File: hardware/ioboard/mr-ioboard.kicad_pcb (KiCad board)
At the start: 0 parts

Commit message: Initial IO board layout
Signed-off-by: gatecat <gatecat@ds0.me>
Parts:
- added AE1: Antenna_Chip, RF_Antenna:Johanson_2450AT43F0100, F.Cu at (105.0, 57.0)
- added C1: 10µ, Capacitor_SMD:C_0805_2012Metric, F.Cu at (120.5, 84.0)
- added C10: 10µ, Capacitor_SMD:C_0805_2012Metric, F.Cu at (111.0, 88.5)
- added C11: 100p, Capacitor_SMD:C_0402_1005Metric, F.Cu at (123.5, 103.0)
- added C12: 1µ, Capacitor_SMD:C_0603_1608Metric, F.Cu at (108.0, 116.5)
- added C13: 10µ, Capacitor_SMD:C_0805_2012Metric, F.Cu at (123.0, 93.0)
- added C14: 10µ, Capacitor_SMD:C_0805_2012Metric, F.Cu at (114.3, 100.5)
- added C15: 10µ, Capacitor_SMD:C_0805_2012Metric, F.Cu at (123.0, 84.0)
- added C16: 10µ, Capacitor_SMD:C_0805_2012Metric, F.Cu at (116.8, 100.5)
- added C17: 10µ, Capacitor_SMD:C_0805_2012Metric, F.Cu at (111.8, 100.5)
- added C18: 470n, Capacitor_SMD:C_0402_1005Metric, F.Cu at (138.5, 69.0)
- added C19: 470n, Capacitor_SMD:C_0402_1005Metric, F.Cu at (136.5, 76.5)
- added C2: 10µ/25V, Capacitor_SMD:C_0805_2012Metric, F.Cu at (125.5, 108.0)
- added C20: 470n, Capacitor_SMD:C_0402_1005Metric, F.Cu at (142.5, 86.5)
- added C21: 10n, Capacitor_SMD:C_0402_1005Metric, F.Cu at (159.5, 89.0)
- added C22: 10µ, Capacitor_SMD:C_0805_2012Metric, F.Cu at (155.5, 92.0)
- added C23: 200p, Capacitor_SMD:C_0402_1005Metric, F.Cu at (135.5, 115.5)
- added C24: 200p, Capacitor_SMD:C_0402_1005Metric, F.Cu at (135.5, 114.0)
- added C25: 10µ, Capacitor_SMD:C_0805_2012Metric, F.Cu at (113.5, 80.0)
- added C26: 10µ, Capacitor_SMD:C_0805_2012Metric, F.Cu at (111.0, 80.0)
- added C27: 10p, Capacitor_SMD:C_0402_1005Metric, F.Cu at (111.0, 64.5)
- added C28: 1p, Capacitor_SMD:C_0402_1005Metric, F.Cu at (109.0, 65.0)
- added C29: 1.2p, Capacitor_SMD:C_0402_1005Metric, F.Cu at (106.0, 65.0)
- added C3: 10µ, Capacitor_SMD:C_0805_2012Metric, F.Cu at (120.5, 93.0)
- added C30: 10µ, Capacitor_SMD:C_0805_2012Metric, F.Cu at (150.5, 99.5)
- added C31: 10µ, Capacitor_SMD:C_0805_2012Metric, F.Cu at (149.0, 96.0)
- added C32: 10µ, Capacitor_SMD:C_0805_2012Metric, F.Cu at (150.6, 93.0)
- added C33: 470n, Capacitor_SMD:C_0402_1005Metric, F.Cu at (132.5, 103.5)
- added C34: 470n, Capacitor_SMD:C_0402_1005Metric, F.Cu at (128.5, 94.5)
- added C35: 470n, Capacitor_SMD:C_0402_1005Metric, F.Cu at (145.5, 87.0)
- added C36: 470n, Capacitor_SMD:C_0402_1005Metric, F.Cu at (128.5, 91.5)
- added C37: 470n, Capacitor_SMD:C_0402_1005Metric, F.Cu at (146.0, 96.0)
- added C38: 470n, Capacitor_SMD:C_0402_1005Metric, F.Cu at (134.5, 86.5)
- added C39: 470n, Capacitor_SMD:C_0402_1005Metric, F.Cu at (146.5, 92.0)
- added C4: 10µ/25V, Capacitor_SMD:C_0805_2012Metric, F.Cu at (124.5, 112.0)
- added C40: 470n, Capacitor_SMD:C_0402_1005Metric, F.Cu at (145.0, 100.5)
- added C41: 470n, Capacitor_SMD:C_0402_1005Metric, F.Cu at (148.0, 99.5)
- added C42: 470n, Capacitor_SMD:C_0402_1005Metric, F.Cu at (132.5, 102.5)
- added C43: 470n, Capacitor_SMD:C_0402_1005Metric, F.Cu at (128.5, 92.5)
- added C44: 10µ, Capacitor_SMD:C_0805_2012Metric, F.Cu at (151.5, 96.0)
- added C45: 470n, Capacitor_SMD:C_0402_1005Metric, F.Cu at (128.5, 95.5)
- added C46: 10µ, Capacitor_SMD:C_0805_2012Metric, F.Cu at (133.5, 80.5)
- added C47: 10µ, Capacitor_SMD:C_0805_2012Metric, F.Cu at (129.0, 84.0)
- added C48: 1µ, Capacitor_SMD:C_0603_1608Metric, F.Cu at (128.5, 97.0)
- added C49: 1u, Capacitor_SMD:C_0603_1608Metric, F.Cu at (149.5, 89.0)
- added C5: 22µ, Capacitor_Tantalum_SMD:CP_EIA-3528-12_Kemet-T, F.Cu at (108.0, 123.0)
- added C50: 1u, Capacitor_SMD:C_0603_1608Metric, F.Cu at (149.5, 85.0)
- added C51: 10µ, Capacitor_SMD:C_0805_2012Metric, F.Cu at (150.6, 103.0)
- added C6: 470n, Capacitor_SMD:C_0402_1005Metric, F.Cu at (138.5, 64.0)
- added C7: 470n, Capacitor_SMD:C_0402_1005Metric, F.Cu at (138.0, 76.5)
- added C8: 10µ, Capacitor_SMD:C_0805_2012Metric, F.Cu at (113.5, 88.5)
- added C9: 100n/25V, Capacitor_SMD:C_0402_1005Metric, F.Cu at (120.0, 112.5)
- added D1: LED_Small, LED_SMD:LED_0805_2012Metric, F.Cu at (138.0, 53.0)
- added D2: LED_Small, LED_SMD:LED_0805_2012Metric, F.Cu at (141.0, 53.0)
- added D3: LED_Small, LED_SMD:LED_0805_2012Metric, F.Cu at (144.0, 53.0)
- added D4: LED_Small, LED_SMD:LED_0805_2012Metric, F.Cu at (153.0, 53.0)
- added FB1: FerriteBead_Small, Inductor_SMD:L_0603_1608Metric, F.Cu at (154.7, 99.5)
- added J1: Conn_01x40_Shielded, meowality:TE_FPC_40pin_p0.5mm_4-1734839-0, F.Cu at (160.0, 70.0)
- added J2: USB_C_Receptacle_USB2.0, Connector_USB:USB_C_Receptacle_GCT_USB4085, F.Cu at (115.0, 124.0)
- added J3: Conn_01x06, Connector_PinHeader_2.54mm:PinHeader_1x06_P2.54mm_Vertical, F.Cu at (103.0, 81.5)
- added J4: Micro_SD_Card_Det, Connector_Card:microSD_HC_Hirose_DM3BT-DSF-PEJS, F.Cu at (155.0, 120.0)
- added J5: Conn_01x04, Connector_PinHeader_2.54mm:PinHeader_1x04_P2.54mm_Vertical, F.Cu at (103.0, 100.0)
- added JP1: CS, Jumper:SolderJumper-3_P1.3mm_Bridged12_Pad1.0x1.5mm, F.Cu at (107.2, 72.0)
- added L1: XFL4015-471MEB, Inductor_SMD:L_Coilcraft_XxL4020, F.Cu at (112.0, 93.0)
- added L2: 2.2u, Inductor_SMD:L_Bourns_SRP7028A_7.3x6.6mm, F.Cu at (115.0, 108.0)
- added L3: XFL4015-471MEB, Inductor_SMD:L_Coilcraft_XxL4020, F.Cu at (112.0, 84.2)
- added L4: 2.7n, Inductor_SMD:L_0402_1005Metric, F.Cu at (107.5, 64.5)
- added MOD1: RTL8189ES_MOD, meowality:RTL8189ES_MOD, F.Cu at (129.5, 73.2)
- added Q1: 2N7002, Package_TO_SOT_SMD:SOT-23, F.Cu at (150.0, 60.0)
- added R1: 10k, Resistor_SMD:R_0402_1005Metric, F.Cu at (117.0, 96.0)
- added R10: 0, Resistor_SMD:R_0402_1005Metric, F.Cu at (119.5, 103.0)
- added R11: 45.3k, Resistor_SMD:R_0402_1005Metric, F.Cu at (120.5, 103.0)
- added R12: 10k, Resistor_SMD:R_0402_1005Metric, F.Cu at (125.5, 103.5)
- added R13: 10k, Resistor_SMD:R_0402_1005Metric, F.Cu at (154.0, 75.5)
- added R14: 10k, Resistor_SMD:R_0402_1005Metric, F.Cu at (135.0, 73.0)
- added R15: 10k, Resistor_SMD:R_0402_1005Metric, F.Cu at (117.0, 86.5)
- added R16: 2.2k, Resistor_SMD:R_0402_1005Metric, F.Cu at (136.0, 122.5)
- added R17: 2.2k, Resistor_SMD:R_0402_1005Metric, F.Cu at (136.0, 123.5)
- added R18: 2.2k, Resistor_SMD:R_0402_1005Metric, F.Cu at (136.0, 124.5)
- added R19: 8.45k, Resistor_SMD:R_0402_1005Metric, F.Cu at (117.0, 79.0)
- added R2: NC, Resistor_SMD:R_0402_1005Metric, F.Cu at (125.5, 105.0)
- added R20: 10k, Resistor_SMD:R_0402_1005Metric, F.Cu at (117.0, 80.5)
- added R21: 10k, Resistor_SMD:R_0402_1005Metric, F.Cu at (146.0, 59.0)
- added R22: 2.2k, Resistor_SMD:R_0402_1005Metric, F.Cu at (154.0, 57.5)
- added R23: 75, Resistor_SMD:R_0402_1005Metric, F.Cu at (146.5, 94.0)
- added R24: 75, Resistor_SMD:R_0402_1005Metric, F.Cu at (146.5, 93.0)
- added R25: 2.2k, Resistor_SMD:R_0402_1005Metric, F.Cu at (128.0, 87.0)
- added R26: 2.2k, Resistor_SMD:R_0402_1005Metric, F.Cu at (129.0, 87.0)
- added R27: 200k, Resistor_SMD:R_0402_1005Metric, F.Cu at (149.5, 87.5)
- added R28: 200k, Resistor_SMD:R_0402_1005Metric, F.Cu at (149.5, 86.5)
- added R3: 2.2k, Resistor_SMD:R_0402_1005Metric, F.Cu at (138.0, 58.5)
- added R4: 2.2k, Resistor_SMD:R_0402_1005Metric, F.Cu at (141.0, 58.5)
- added R5: 15k, Resistor_SMD:R_0402_1005Metric, F.Cu at (117.0, 89.0)
- added R6: 10k, Resistor_SMD:R_0402_1005Metric, F.Cu at (117.0, 90.5)
- added R7: 2.2k, Resistor_SMD:R_0402_1005Metric, F.Cu at (144.0, 58.5)
- added R8: 0, Resistor_SMD:R_0402_1005Metric, F.Cu at (120.0, 113.5)
- added R9: 20k, Resistor_SMD:R_0402_1005Metric, F.Cu at (122.5, 103.0)
- added RN1: 47k, Resistor_SMD:R_Array_Convex_4x0402, F.Cu at (161.5, 103.5)
- added RN2: 47k, Resistor_SMD:R_Array_Convex_4x0402, F.Cu at (161.5, 108.5)
- added RN3: 47k, Resistor_SMD:R_Array_Convex_4x0402, F.Cu at (135.0, 70.2)
- added RN4: 47k, Resistor_SMD:R_Array_Convex_4x0402, F.Cu at (135.0, 63.8)
- added SW1: SW_Push, Button_Switch_SMD:SW_SPST_B3U-1000P, F.Cu at (103.0, 115.0)
- added TP1: EN, TestPoint:TestPoint_Pad_D2.0mm, F.Cu at (129.0, 105.5)
- added TP2: TestPoint, TestPoint:TestPoint_Pad_D2.0mm, F.Cu at (129.5, 126.0)
- added U1: TPS62822, meowality:TI_VSON-HR_1.5x2mm_p0.5mm, F.Cu at (117.0, 93.0)
- added U10: F1C200S, meowality:QFN-88_EP_10x10_Pitch0.4mm, F.Cu at (138.2, 94.2)
- added U2: TPS56637, meowality:VQFN10-HR, F.Cu at (122.0, 108.0)
- added U3: TPD2E2U06, Package_TO_SOT_SMD:SOT-553, F.Cu at (116.0, 119.5)
- added U4: DS90C363, Package_SO:TSSOP-48_8x12.5mm_P0.5mm, F.Cu at (146.0, 71.0)
- added U5: TPD2E2U06, Package_TO_SOT_SMD:SOT-553, F.Cu at (120.0, 119.5)
- added U6: LD3985M28R_SOT23, Package_TO_SOT_SMD:SOT-23-5, F.Cu at (159.5, 92.0)
- added U7: TPS62822, meowality:TI_VSON-HR_1.5x2mm_p0.5mm, F.Cu at (117.0, 84.0)
- added U8: FUSB302BMPX, Package_DFN_QFN:WQFN-14-1EP_2.5x2.5mm_P0.5mm_EP1.45x1.45mm, F.Cu at (133.0, 119.0)
- added U9: TPD2E2U06, Package_TO_SOT_SMD:SOT-553, F.Cu at (126.5, 119.5)
- added Y1: 24MHz, Oscillator:Oscillator_SMD_EuroQuartz_XO32-4Pin_3.2x2.5mm, F.Cu at (137.0, 103.5)
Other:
- board outline added: 65 x 80 mm
- copper layers 0 -> 2

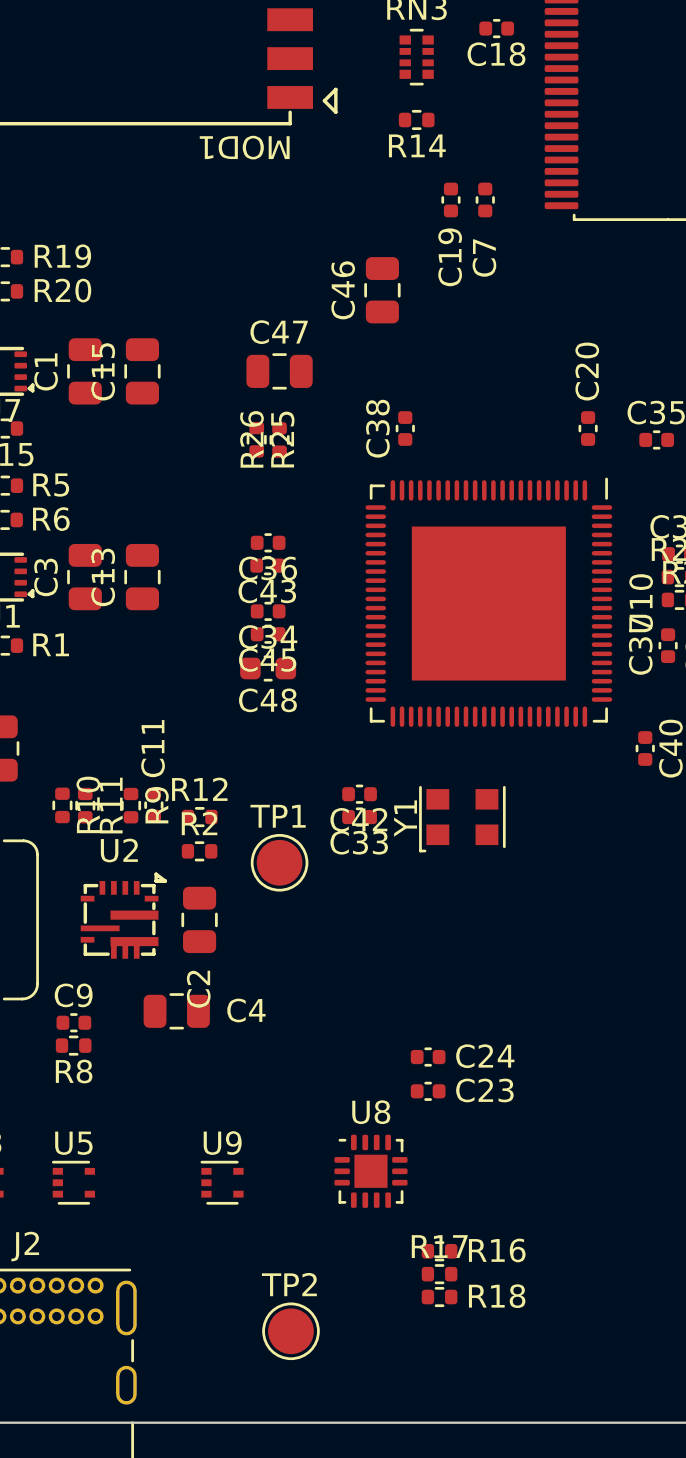
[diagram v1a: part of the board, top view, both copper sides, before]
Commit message: Add a few missing parts to IO board
Signed-off-by: gatecat <gatecat@ds0.me>
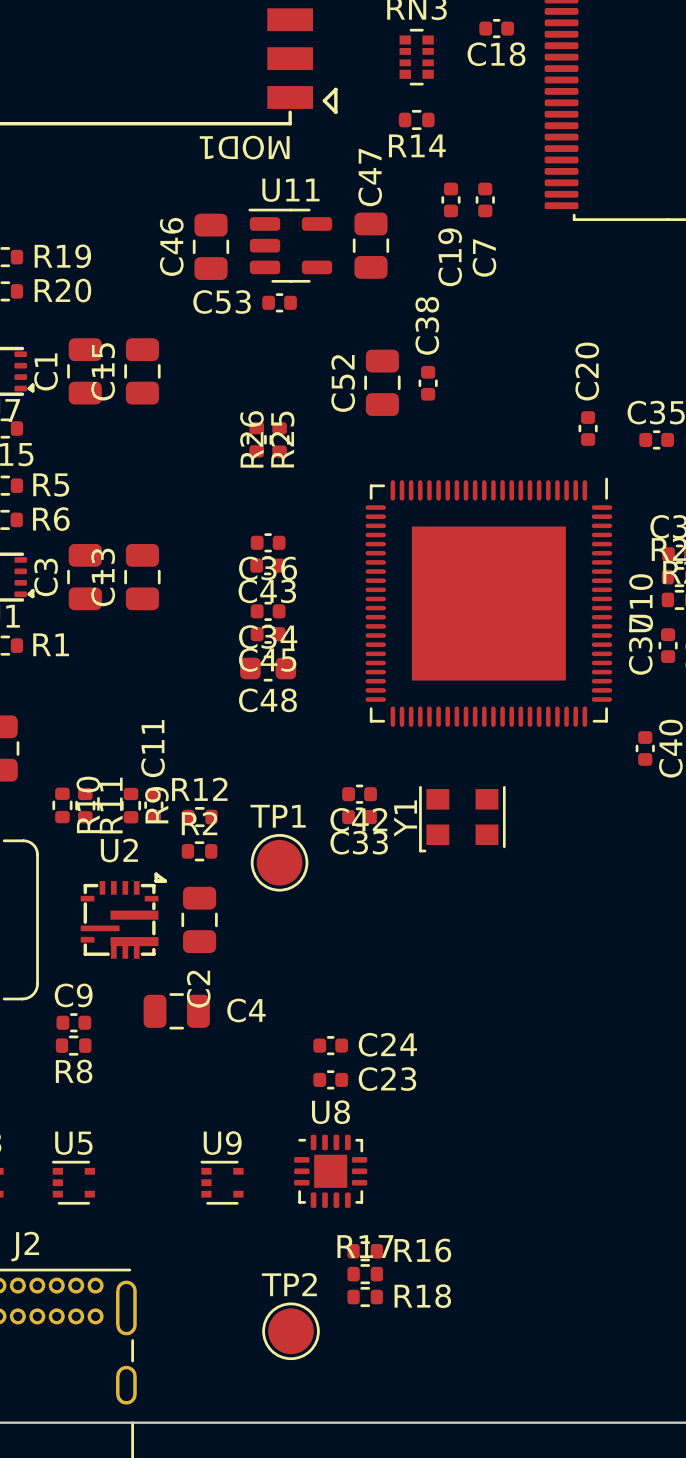
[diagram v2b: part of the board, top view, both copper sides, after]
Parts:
- added C52: 10µ, Capacitor_SMD:C_0805_2012Metric, F.Cu at (133.5, 84.5)
- added C53: 10n, Capacitor_SMD:C_0402_1005Metric, F.Cu at (129.0, 81.0)
- added U11: LD3985M25R_SOT23, Package_TO_SOT_SMD:SOT-23-5, F.Cu at (129.5, 78.5)
- moved C46 7.74 mm to (126.0, 78.5)
- moved C47 6.80 mm to (133.0, 78.5), turned to -90 degrees
- moved C23 4.29 mm to (131.2, 115.0)
- moved C24 4.29 mm to (131.2, 113.5)
- moved R16 3.25 mm to (132.7, 122.5)
- moved R17 3.25 mm to (132.7, 123.5)
- moved R18 3.25 mm to (132.7, 124.5)
- moved C38 2.22 mm to (135.5, 84.5)
- moved U8 1.76 mm to (131.2, 119.0)

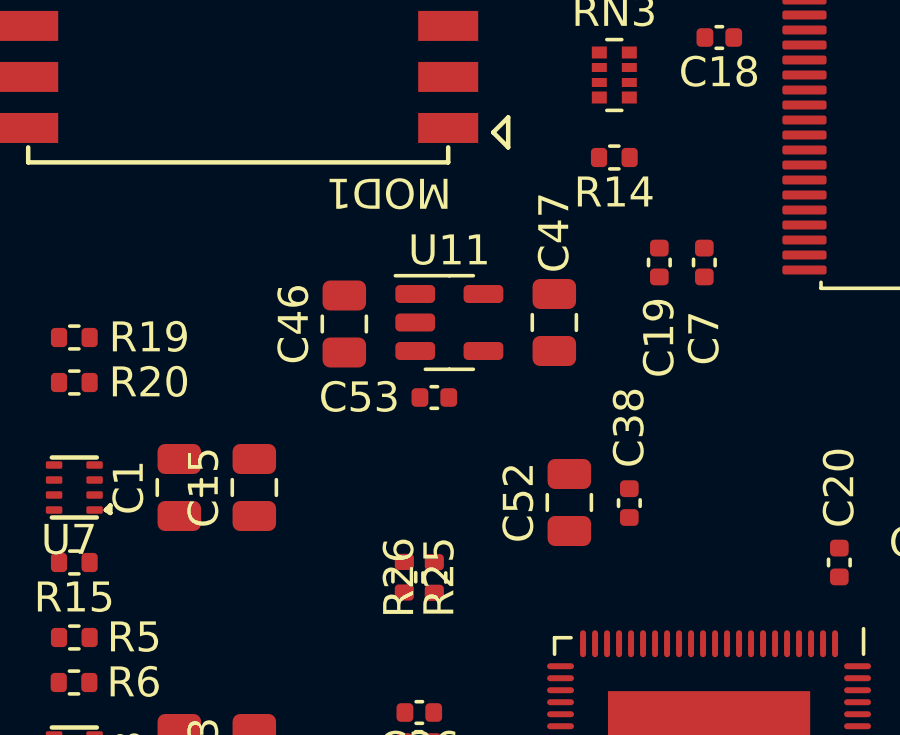
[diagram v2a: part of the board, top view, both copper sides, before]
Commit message: Fix IO board 2.5V supply
Signed-off-by: gatecat <gatecat@ds0.me>
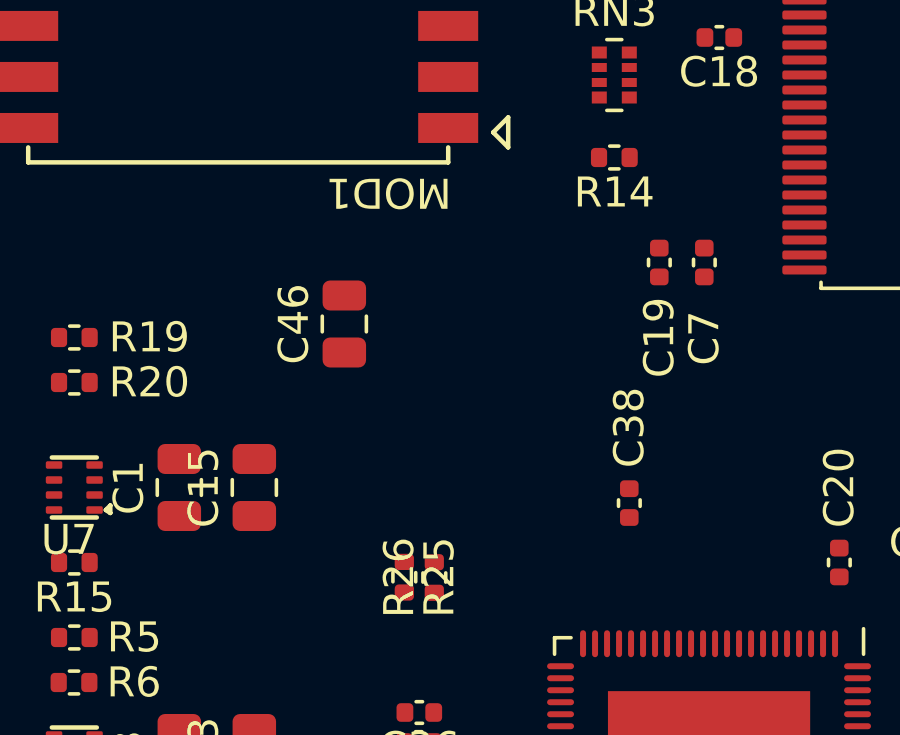
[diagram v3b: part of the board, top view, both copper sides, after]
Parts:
- removed C47, C52: 10µ, Capacitor_SMD:C_0805_2012Metric
- removed C53: 10n, Capacitor_SMD:C_0402_1005Metric
- removed U11: LD3985M25R_SOT23, Package_TO_SOT_SMD:SOT-23-5
- R5: value 15k -> 31.6k
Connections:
- C10 pad 1: +1V5 -> +2V5
- C8 pad 1: +1V5 -> +2V5
- L1 pad 2: +1V5 -> +2V5
- R5 pad 1: +1V5 -> +2V5

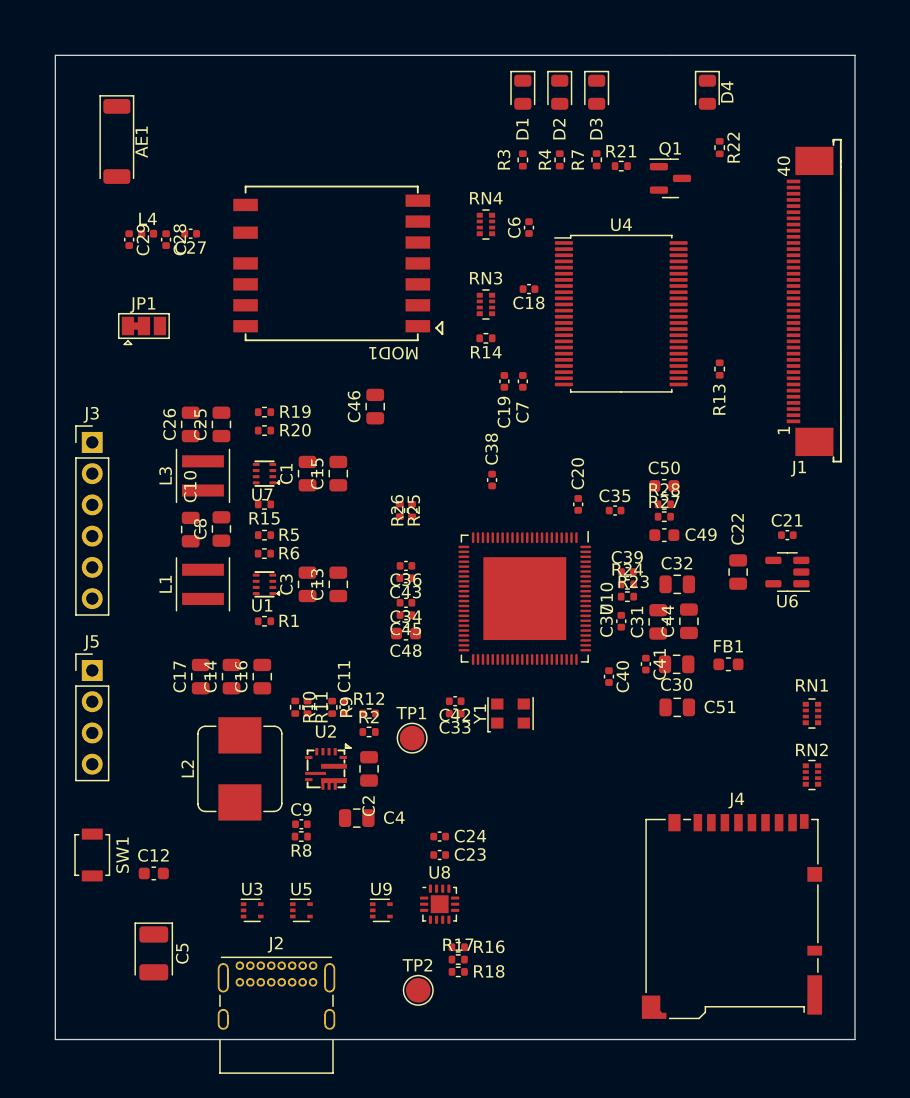
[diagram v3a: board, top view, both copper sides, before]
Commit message: Add VLED buck regulator to IO board
Signed-off-by: gatecat <gatecat@ds0.me>
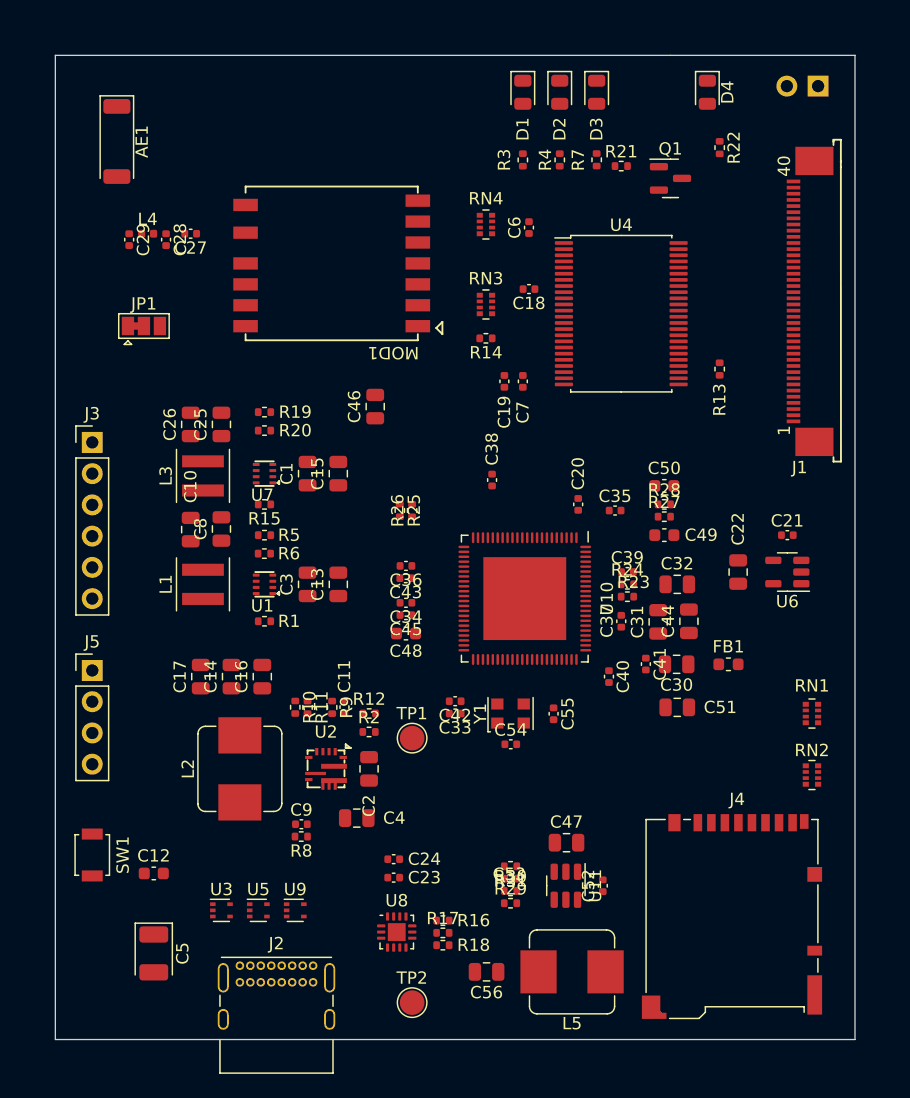
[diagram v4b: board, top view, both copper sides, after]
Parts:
- added C47: 10µ/25V, Capacitor_SMD:C_0805_2012Metric, F.Cu at (141.6, 114.0)
- added C52: 100n, Capacitor_SMD:C_0402_1005Metric, F.Cu at (144.5, 117.5)
- added C53: 100p, Capacitor_SMD:C_0402_1005Metric, F.Cu at (137.0, 116.9)
- added C54: 12p, Capacitor_SMD:C_0402_1005Metric, F.Cu at (137.0, 106.0)
- added C55: 12p, Capacitor_SMD:C_0402_1005Metric, F.Cu at (140.5, 103.5)
- added C56: 10µ, Capacitor_SMD:C_0805_2012Metric, F.Cu at (135.1, 124.5)
- added J6: Conn_01x02, Connector_PinHeader_2.54mm:PinHeader_1x02_P2.54mm_Vertical, B.Cu at (162.0, 52.5)
- added L5: 15u, Inductor_SMD:L_Bourns_SRP7028A_7.3x6.6mm, F.Cu at (142.0, 124.5)
- added R29: 49.9, Resistor_SMD:R_0402_1005Metric, F.Cu at (137.0, 118.9)
- added R30: 100k, Resistor_SMD:R_0402_1005Metric, F.Cu at (137.0, 117.9)
- added R31: 13.3k, Resistor_SMD:R_0402_1005Metric, F.Cu at (137.0, 115.9)
- added U11: TPS54202DDC, Package_TO_SOT_SMD:SOT-23-6, F.Cu at (141.5, 117.5)
- moved U9 7.00 mm to (119.5, 119.5)
- moved C23 4.17 mm to (127.5, 116.8)
- moved C24 4.17 mm to (127.5, 115.3)
- moved U8 4.16 mm to (127.8, 121.3)
- moved U5 3.50 mm to (116.5, 119.5)
- moved R16 2.50 mm to (131.5, 120.3)
- moved R17 2.50 mm to (131.5, 121.3)
- moved R18 2.50 mm to (131.5, 122.3)
- moved U3 2.50 mm to (113.5, 119.5)
- moved TP2 1.12 mm to (129.0, 127.0)

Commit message: IO board routing
Signed-off-by: gatecat <gatecat@ds0.me>
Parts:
- moved C55 4.07 mm to (137.4, 106.2)
- moved C41 3.03 mm to (146.0, 101.8)
- moved C40 1.95 mm to (143.5, 101.8)
- moved C54 1.90 mm to (135.1, 106.2), turned to -90 degrees
- moved Y1 0.86 mm to (136.1, 103.5)
- moved C37 0.50 mm to (146.0, 96.5)
- moved C38 0.49 mm to (135.0, 84.5)
- turned L4 to 180 degrees
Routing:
- net /LCD_D6: track 0.00 -> 48.6 mm
- net /LCD_D3: track 0.00 -> 43.6 mm
- net /LCD_D11: track 0.00 -> 38.6 mm
- net /LCD_D7: track 0.00 -> 35.3 mm
- net +3V3: track 0.00 -> 34.8 mm
- net +2V5: track 0.00 -> 34.8 mm, vias 0 -> 2
- net /LCD_D10: track 0.00 -> 34.7 mm
- net /LCD_D18: track 0.00 -> 34.6 mm
- net /SDCARD_D1: track 0.00 -> 33.6 mm
- net /LCD_D12: track 0.00 -> 32.5 mm
- net /LCD_D5: track 0.00 -> 32.3 mm
- net /LCD_D4: track 0.00 -> 31.6 mm
- net /LCD_D13: track 0.00 -> 31.4 mm
- net /LCD_D14: track 0.00 -> 30.5 mm
- net /SDCARD_D0: track 0.00 -> 30.2 mm
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- added copper zone on F.Cu, net /VBUS
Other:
- copper layers 2 -> 4

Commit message: IO board routing
Signed-off-by: gatecat <gatecat@ds0.me>
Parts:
- moved C46 4.74 mm to (130.7, 79.4)
- moved C9 2.24 mm to (118.0, 113.5), turned to 180 degrees
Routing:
- net /WIFI_CMD: track 5.60 -> 68.7 mm, vias 0 -> 3
- net /LED2: track 0.00 -> 61.8 mm, vias 0 -> 2
- net /LED1: track 0.00 -> 61.8 mm, vias 0 -> 2
- net +3V3: track 34.8 -> 95.5 mm, vias 0 -> 3
- net /WIFI_CLK: track 6.14 -> 65.4 mm, vias 0 -> 2
- net /LED0: track 0.00 -> 54.8 mm, vias 0 -> 2
- net /WIFI_D0: track 14.0 -> 68.2 mm, vias 0 -> 2
- net GND: track 7.39 -> 59.3 mm, vias 2 -> 14
- net /DBG_TX: track 0.00 -> 40.8 mm, vias 0 -> 2
- net /DBG_RX: track 0.00 -> 39.5 mm, vias 0 -> 2
- net /LCD_CLK: track 0.00 -> 33.5 mm, vias 0 -> 2
- net /LCD_DE: track 3.14 -> 36.2 mm, vias 0 -> 2
- net Net-(C52-Pad2): track 0.00 -> 16.2 mm
- net /SDCARD_D2: track 26.1 -> 40.0 mm, vias 1 -> 2
- net Net-(JP1-Pad2): track 0.00 -> 12.0 mm
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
